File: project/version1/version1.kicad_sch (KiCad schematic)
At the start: 6 parts, among them IC1 ESP32-S3-WROOM-1-N16R2, IC2 TJA1050T_CM,118, IC3 ADS1115LIDGSR

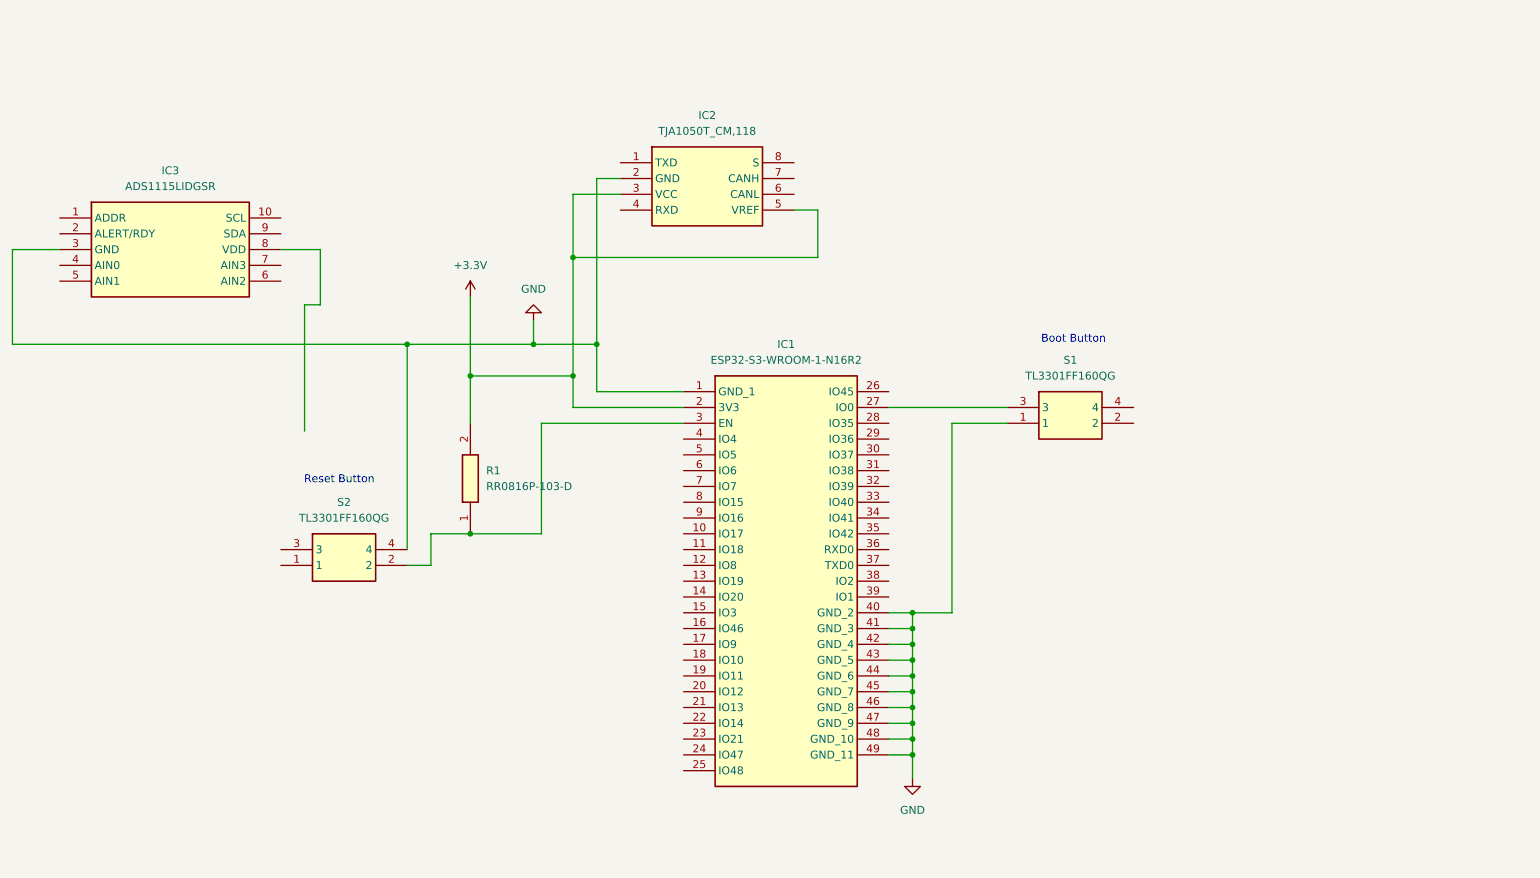
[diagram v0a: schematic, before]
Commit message: placed initial components, leds, etc... Started working on routing the tracks
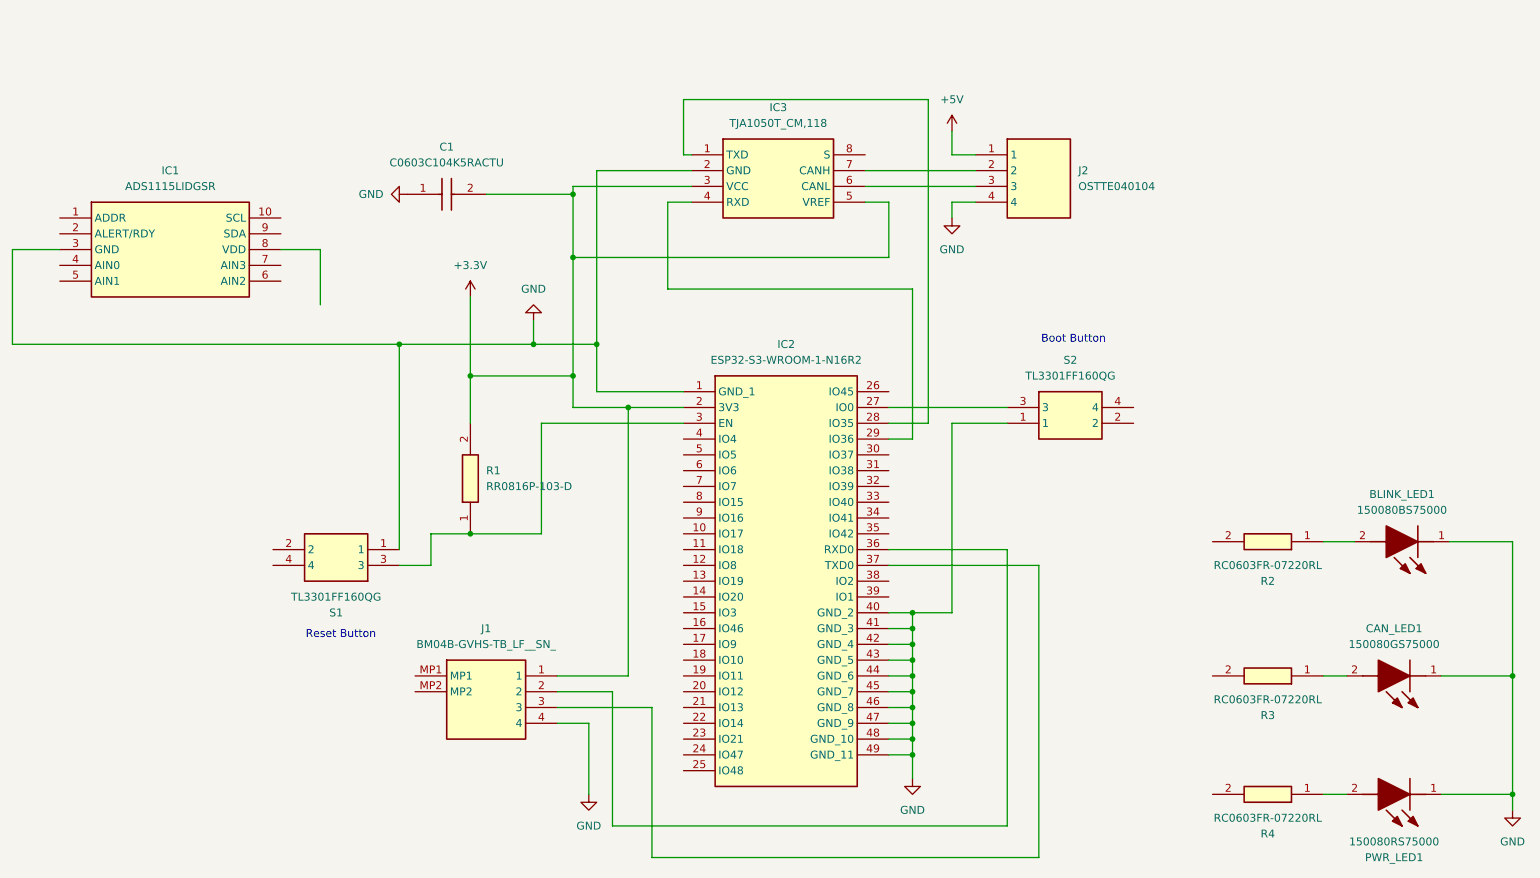
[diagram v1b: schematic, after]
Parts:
- added BLINK_LED1: 150080BS75000, LEDC2012X70N, symbol 150080BS75000:150080BS75000
- added C1: C0603C104K5RACTU, C0603, symbol C0603C104K5RACTU:C0603C104K5RACTU
- added CAN_LED1: 150080GS75000, LEDM2012X70N, symbol 150080GS75000:150080GS75000
- added J1: BM04B-GVHS-TB_LF__SN_, BM04BGVHSTBLFSN, symbol BM04B-GVHS-TB_LF__SN_:BM04B-GVHS-TB_LF__SN_
- added J2: OSTTE040104, OSTTE040104, symbol OSTTE040104:OSTTE040104
- added PWR_LED1: 150080RS75000, LEDC2012X70N, symbol 150080RS75000:150080RS75000
- added R2, R3, R4: RC0603FR-07220RL, RESC1608X55N, symbol RC0603FR-07220RL:RC0603FR-07220RL
- renumbered IC3 to IC1, IC1 to IC2, IC2 to IC3, S2 to S1, S1 to S2
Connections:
- net +3.3V: now also C1.2, J1.1
- net GND: now also S1.1, BLINK_LED1.1 (K), C1.1, CAN_LED1.1 (K), J1.4, J2.4, PWR_LED1.1 (K); no longer S1.4
- net at IC2.3 (EN), R1.1 (R1): now also S1.3; no longer S1.2
- net at IC2.28 (IO35): now also IC3.1 (TXD)
- net at IC2.29 (IO36): now also IC3.4 (RXD)
- net at IC2.36 (RXD0): now also J1.2
- net at IC2.37 (TXD0): now also J1.3
- net at IC3.6 (CANL): now also J2.3
- net at IC3.7 (CANH): now also J2.2
- new net: PWR_LED1.2 (A), R4.1
- new net: BLINK_LED1.2 (A), R2.1
- new net: CAN_LED1.2 (A), R3.1
- new net +5V: J2.1
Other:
- moved on the sheet: IC3, S1

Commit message: added voltage regulator
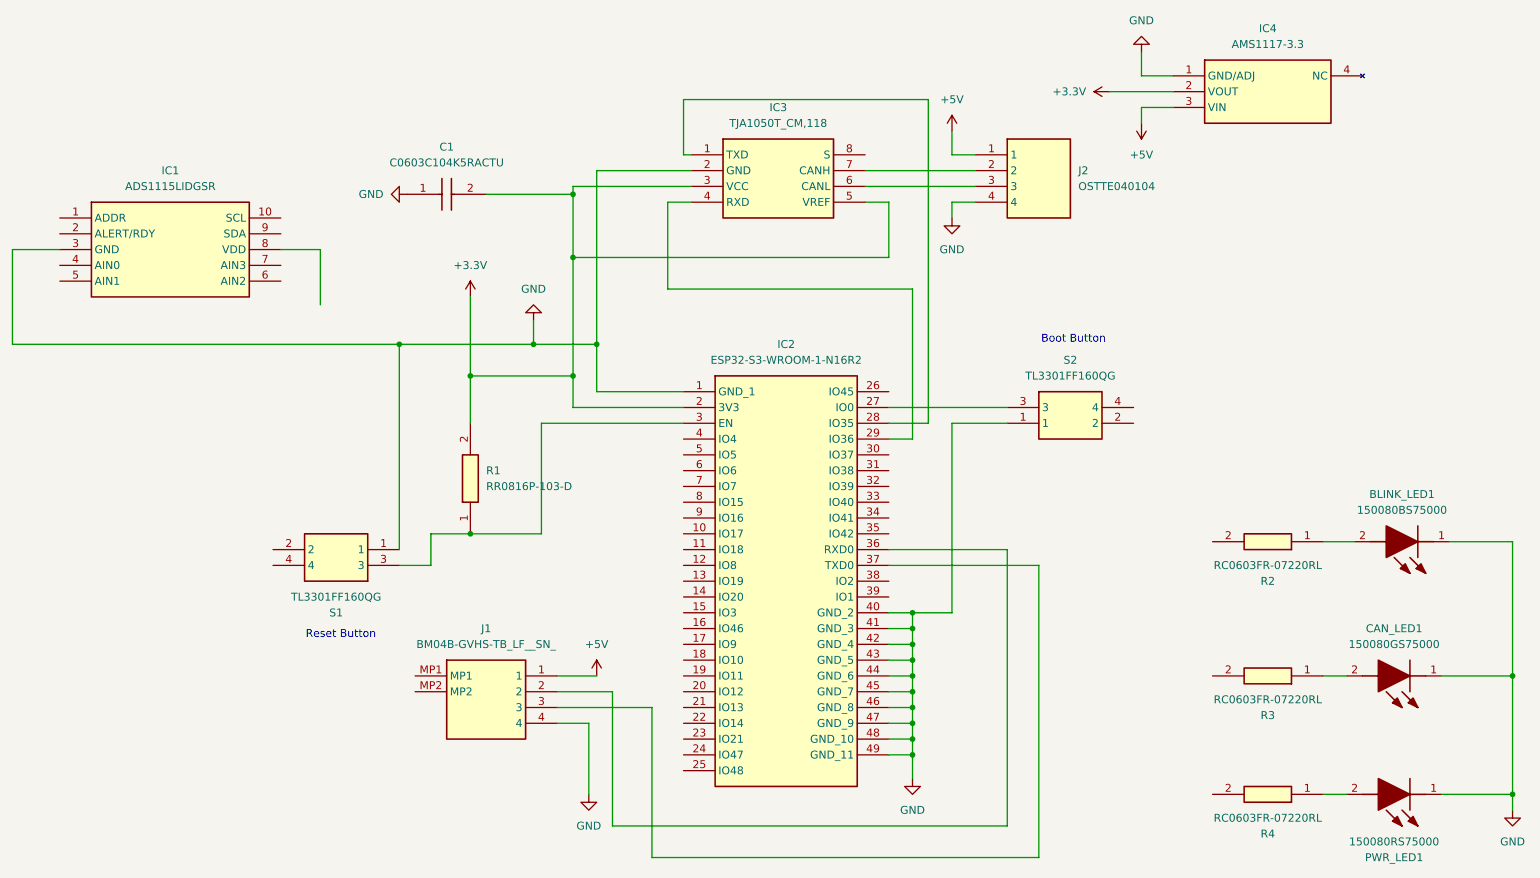
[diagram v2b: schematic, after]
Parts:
- added IC4: AMS1117-3.3, SOT229P700X180-4N, symbol AMS1117-3_3:AMS1117-3.3
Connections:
- net +3.3V: now also IC4.2 (VOUT); no longer J1.1
- net +5V: now also J1.1, IC4.3 (VIN)
- net GND: now also IC4.1 (GND/ADJ)
